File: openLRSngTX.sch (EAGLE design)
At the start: 31 parts, among them IC1 RFM23BPSMD, J1 AVR_SPI_PRG_6PTH, Q1 MMBT2222, U1 ATMEGA328P, X1 BU-SMA-V, Y1 16MHz

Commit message: cleanups
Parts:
- R1, R2, R3, R4, R5, R6, R7, R8: device SparkFun-Resistors:RESISTOR0402-RES -> SparkFun-Resistors:RESISTOR0805-RES
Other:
- moved on the sheet: C7, S1
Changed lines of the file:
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@@
 <part name="JP3" library="SparkFun-Connectors" deviceset="M04" device="PTH" value="I2C"/>
 <part name="Q1" library="SparkFun-DiscreteSemi" deviceset="TRANSISTOR_NPN" device="SOT23-3" value="MMBT2222"/>
-<part name="R1" library="SparkFun-Resistors" deviceset="RESISTOR" device="0402-RES" value="10k"/>
-<part name="R2" library="SparkFun-Resistors" deviceset="RESISTOR" device="0402-RES" value="1k"/>
-<part name="R3" library="SparkFun-Resistors" deviceset="RESISTOR" device="0402-RES" value="1k"/>
-<part name="R4" library="SparkFun-Resistors" deviceset="RESISTOR" device="0402-RES" value="220R"/>
-<part name="R5" library="SparkFun-Resistors" deviceset="RESISTOR" device="0402-RES" value="220R"/>
+<part name="R1" library="SparkFun-Resistors" deviceset="RESISTOR" device="0805-RES" value="10k"/>
+<part name="R2" library="SparkFun-Resistors" deviceset="RESISTOR" device="0805-RES" value="1k"/>
+<part name="R3" library="SparkFun-Resistors" deviceset="RESISTOR" device="0805-RES" value="1k"/>
+<part name="R4" library="SparkFun-Resistors" deviceset="RESISTOR" device="0805-RES" value="220R"/>
+<part name="R5" library="SparkFun-Resistors" deviceset="RESISTOR" device="0805-RES" value="220R"/>
 <part name="LED1" library="SparkFun-LED" deviceset="LED" device="3MM" value="RED"/>
 <part name="LED2" library="SparkFun-LED" deviceset="LED" device="3MM" value="GRN"/>
@@
 <part name="C6" library="SparkFun-Capacitors" deviceset="CAP" device="0805" value="1uF"/>
 <part name="C7" library="SparkFun-Capacitors" deviceset="CAP" device="0805" value="100n"/>
-<part name="R6" library="SparkFun-Resistors" deviceset="RESISTOR" device="0402-RES" value="1k"/>
+<part name="R6" library="SparkFun-Resistors" deviceset="RESISTOR" device="0805-RES" value="1k"/>
 <part name="SUPPLY5" library="SparkFun-Aesthetics" deviceset="VCC" device=""/>
 <part name="C8" library="SparkFun-Capacitors" deviceset="CAP" device="0805" value="100n"/>
 <part name="GND7" library="SparkFun-Aesthetics" deviceset="GND" device=""/>
 <part name="S1" library="SparkFun-Electromechanical" deviceset="SWITCH-MOMENTARY-2" device="SMD"/>
-<part name="R7" library="SparkFun-Resistors" deviceset="RESISTOR" device="0402-RES" value="1k"/>
+<part name="R7" library="SparkFun-Resistors" deviceset="RESISTOR" device="0805-RES" value="1k"/>
 <part name="JP5" library="SparkFun-Connectors" deviceset="M03" device="PTH" value="mode"/>
-<part name="R8" library="SparkFun-Resistors" deviceset="RESISTOR" device="0402-RES" value="1k"/>
+<part name="R8" library="SparkFun-Resistors" deviceset="RESISTOR" device="0805-RES" value="1k"/>
 </parts>
 <sheets>
@@
 <instance part="JP4" gate="G$1" x="-12.7" y="66.04"/>
 <instance part="C6" gate="G$1" x="111.76" y="93.98"/>
-<instance part="C7" gate="G$1" x="104.14" y="93.98"/>
+<instance part="C7" gate="G$1" x="119.38" y="93.98"/>
 <instance part="R6" gate="G$1" x="106.68" y="63.5" rot="R90"/>
 <instance part="SUPPLY5" gate="1" x="106.68" y="71.12"/>
 <instance part="C8" gate="G$1" x="30.48" y="76.2" rot="R90"/>
 <instance part="GND7" gate="1" x="25.4" y="71.12"/>
-<instance part="S1" gate="G$1" x="106.68" y="86.36"/>
+<instance part="S1" gate="G$1" x="106.68" y="91.44"/>
 <instance part="R7" gate="G$1" x="10.16" y="48.26" smashed="yes">
 <attribute name="NAME" x="6.35" y="44.6786" size="1.778" layer="95"/>
@@
 <wire x1="111.76" y1="68.58" x2="111.76" y2="83.82" width="0.1524" layer="91"/>
 <pinref part="C7" gate="G$1" pin="2"/>
-<wire x1="111.76" y1="83.82" x2="111.76" y2="86.36" width="0.1524" layer="91"/>
-<wire x1="111.76" y1="86.36" x2="111.76" y2="91.44" width="0.1524" layer="91"/>
-<wire x1="111.76" y1="91.44" x2="104.14" y2="91.44" width="0.1524" layer="91"/>
+<wire x1="111.76" y1="83.82" x2="111.76" y2="91.44" width="0.1524" layer="91"/>
+<wire x1="111.76" y1="91.44" x2="119.38" y2="91.44" width="0.1524" layer="91"/>
+<pinref part="S1" gate="G$1" pin="2"/>
 <junction x="111.76" y="91.44"/>
-<pinref part="S1" gate="G$1" pin="2"/>
-<junction x="111.76" y="86.36"/>
 <pinref part="JP5" gate="G$1" pin="2"/>
 <wire x1="96.52" y1="101.6" x2="96.52" y2="83.82" width="0.1524" layer="91"/>
@@
 <pinref part="C7" gate="G$1" pin="1"/>
 <pinref part="C6" gate="G$1" pin="1"/>
-<wire x1="104.14" y1="99.06" x2="111.76" y2="99.06" width="0.1524" layer="91"/>
-<wire x1="111.76" y1="99.06" x2="127" y2="99.06" width="0.1524" layer="91"/>
+<wire x1="111.76" y1="99.06" x2="119.38" y2="99.06" width="0.1524" layer="91"/>
 <junction x="127" y="99.06"/>
-<junction x="111.76" y="99.06"/>
+<junction x="119.38" y="99.06"/>
+<wire x1="119.38" y1="99.06" x2="127" y2="99.06" width="0.1524" layer="91"/>
 </segment>
 <segment>
@@
 <segment>
 <pinref part="S1" gate="G$1" pin="1"/>
-<wire x1="101.6" y1="86.36" x2="101.6" y2="91.44" width="0.1524" layer="91"/>
 <pinref part="U1" gate="G$1" pin="PC0(ADC0)"/>
 <wire x1="101.6" y1="91.44" x2="91.44" y2="91.44" width="0.1524" layer="91"/>

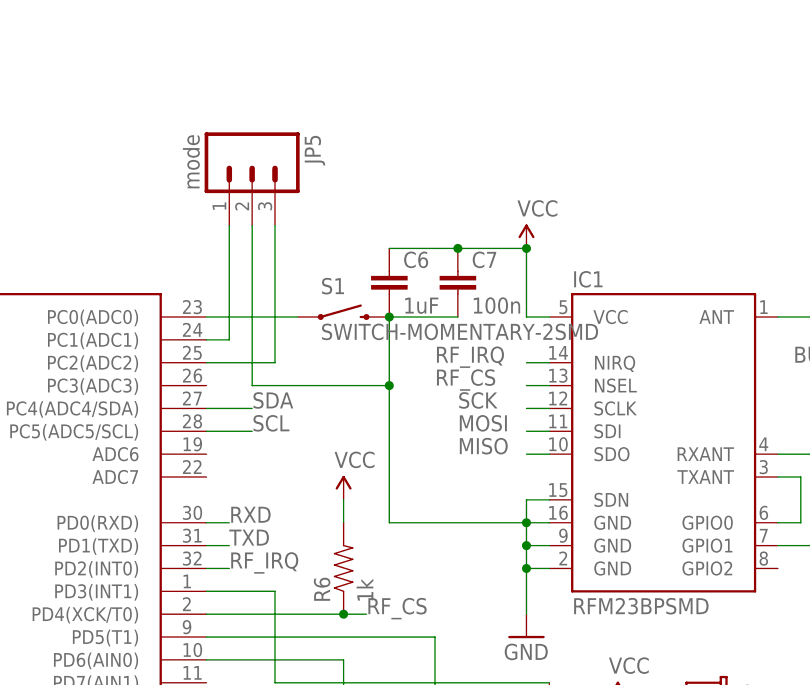
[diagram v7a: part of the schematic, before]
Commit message: Add possibility for wired boind button.
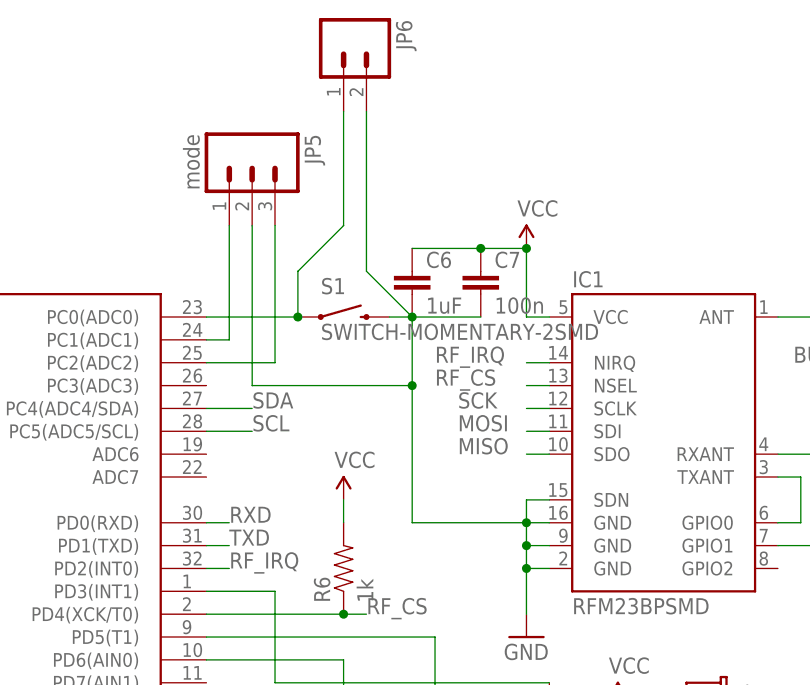
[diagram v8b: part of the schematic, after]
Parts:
- added JP6: (no value), SparkFun-Connectors:M02PTH
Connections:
- net GND: now also JP6.2
- net N$15: now also JP6.1
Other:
- moved on the sheet: C6, C7
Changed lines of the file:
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@@
 <part name="JP5" library="SparkFun-Connectors" deviceset="M03" device="PTH" value="mode"/>
 <part name="R8" library="SparkFun-Resistors" deviceset="RESISTOR" device="0805-RES" value="1k"/>
+<part name="JP6" library="SparkFun-Connectors" deviceset="M02" device="PTH"/>
 </parts>
 <sheets>
@@
 <instance part="JP1" gate="G$1" x="-12.7" y="45.72"/>
 <instance part="JP4" gate="G$1" x="-12.7" y="66.04"/>
-<instance part="C6" gate="G$1" x="111.76" y="93.98"/>
-<instance part="C7" gate="G$1" x="119.38" y="93.98"/>
+<instance part="C6" gate="G$1" x="114.3" y="93.98"/>
+<instance part="C7" gate="G$1" x="121.92" y="93.98"/>
 <instance part="R6" gate="G$1" x="106.68" y="63.5" rot="R90"/>
 <instance part="SUPPLY5" gate="1" x="106.68" y="71.12"/>
@@
 <attribute name="VALUE" x="3.81" y="52.578" size="1.778" layer="96"/>
 </instance>
+<instance part="JP6" gate="G$1" x="106.68" y="121.92" rot="R270"/>
 </instances>
 <busses>
@@
 <wire x1="127" y1="71.12" x2="129.54" y2="71.12" width="0.1524" layer="91"/>
 <junction x="127" y="68.58"/>
-<wire x1="127" y1="68.58" x2="111.76" y2="68.58" width="0.1524" layer="91"/>
+<wire x1="127" y1="68.58" x2="114.3" y2="68.58" width="0.1524" layer="91"/>
 <pinref part="C6" gate="G$1" pin="2"/>
-<wire x1="111.76" y1="68.58" x2="111.76" y2="83.82" width="0.1524" layer="91"/>
+<wire x1="114.3" y1="68.58" x2="114.3" y2="83.82" width="0.1524" layer="91"/>
 <pinref part="C7" gate="G$1" pin="2"/>
-<wire x1="111.76" y1="83.82" x2="111.76" y2="91.44" width="0.1524" layer="91"/>
-<wire x1="111.76" y1="91.44" x2="119.38" y2="91.44" width="0.1524" layer="91"/>
+<wire x1="114.3" y1="83.82" x2="114.3" y2="91.44" width="0.1524" layer="91"/>
+<wire x1="114.3" y1="91.44" x2="121.92" y2="91.44" width="0.1524" layer="91"/>
 <pinref part="S1" gate="G$1" pin="2"/>
-<junction x="111.76" y="91.44"/>
+<junction x="114.3" y="91.44"/>
 <pinref part="JP5" gate="G$1" pin="2"/>
 <wire x1="96.52" y1="101.6" x2="96.52" y2="83.82" width="0.1524" layer="91"/>
-<wire x1="96.52" y1="83.82" x2="111.76" y2="83.82" width="0.1524" layer="91"/>
-<junction x="111.76" y="83.82"/>
+<wire x1="96.52" y1="83.82" x2="114.3" y2="83.82" width="0.1524" layer="91"/>
+<junction x="114.3" y="83.82"/>
+<wire x1="114.3" y1="91.44" x2="111.76" y2="91.44" width="0.1524" layer="91"/>
+<wire x1="114.3" y1="91.44" x2="109.22" y2="96.52" width="0.1524" layer="91"/>
+<pinref part="JP6" gate="G$1" pin="2"/>
+<wire x1="109.22" y1="96.52" x2="109.22" y2="114.3" width="0.1524" layer="91"/>
 </segment>
 <segment>
@@
 <pinref part="C7" gate="G$1" pin="1"/>
 <pinref part="C6" gate="G$1" pin="1"/>
-<wire x1="111.76" y1="99.06" x2="119.38" y2="99.06" width="0.1524" layer="91"/>
+<wire x1="114.3" y1="99.06" x2="121.92" y2="99.06" width="0.1524" layer="91"/>
 <junction x="127" y="99.06"/>
-<junction x="119.38" y="99.06"/>
-<wire x1="119.38" y1="99.06" x2="127" y2="99.06" width="0.1524" layer="91"/>
+<junction x="121.92" y="99.06"/>
+<wire x1="121.92" y1="99.06" x2="127" y2="99.06" width="0.1524" layer="91"/>
 </segment>
 <segment>
@@
 <pinref part="U1" gate="G$1" pin="PC0(ADC0)"/>
 <wire x1="101.6" y1="91.44" x2="91.44" y2="91.44" width="0.1524" layer="91"/>
-</segment>
-</net>
+<wire x1="101.6" y1="91.44" x2="101.6" y2="96.52" width="0.1524" layer="91"/>
+<wire x1="101.6" y1="96.52" x2="106.68" y2="101.6" width="0.1524" layer="91"/>
+<pinref part="JP6" gate="G$1" pin="1"/>
+<wire x1="106.68" y1="101.6" x2="106.68" y2="114.3" width="0.1524" layer="91"/>
+<junction x="101.6" y="91.44"/>
+</segment>
+</net>
